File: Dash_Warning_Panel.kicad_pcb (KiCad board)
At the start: 2 copper layers, 60 x 40 mm, 33 parts, among them J1 Conn, U1 TLC6C598, U2 TPS22810

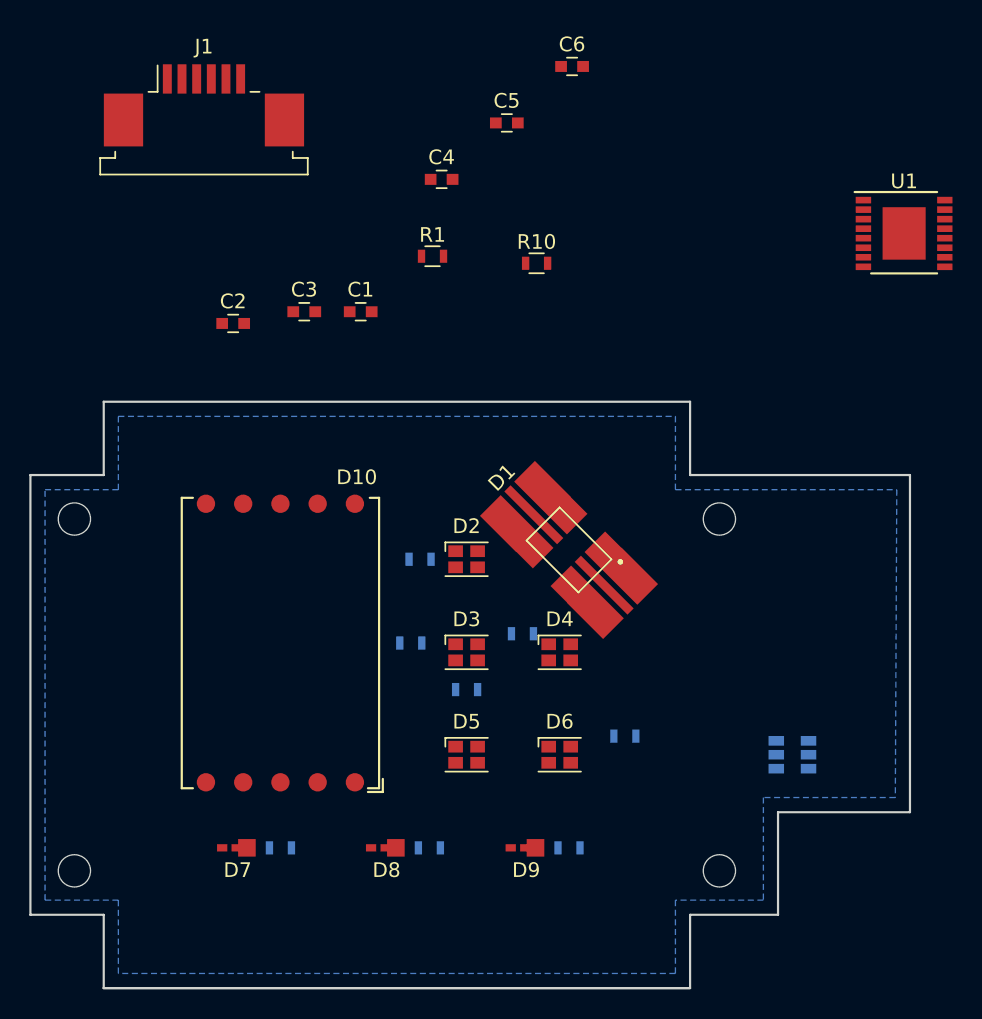
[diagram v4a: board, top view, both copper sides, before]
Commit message: 2020 Initial Design
2020 Initial Design Submission:
Connector changed to 8 pin Molex 90 degree KK
Added Seven Segment Display
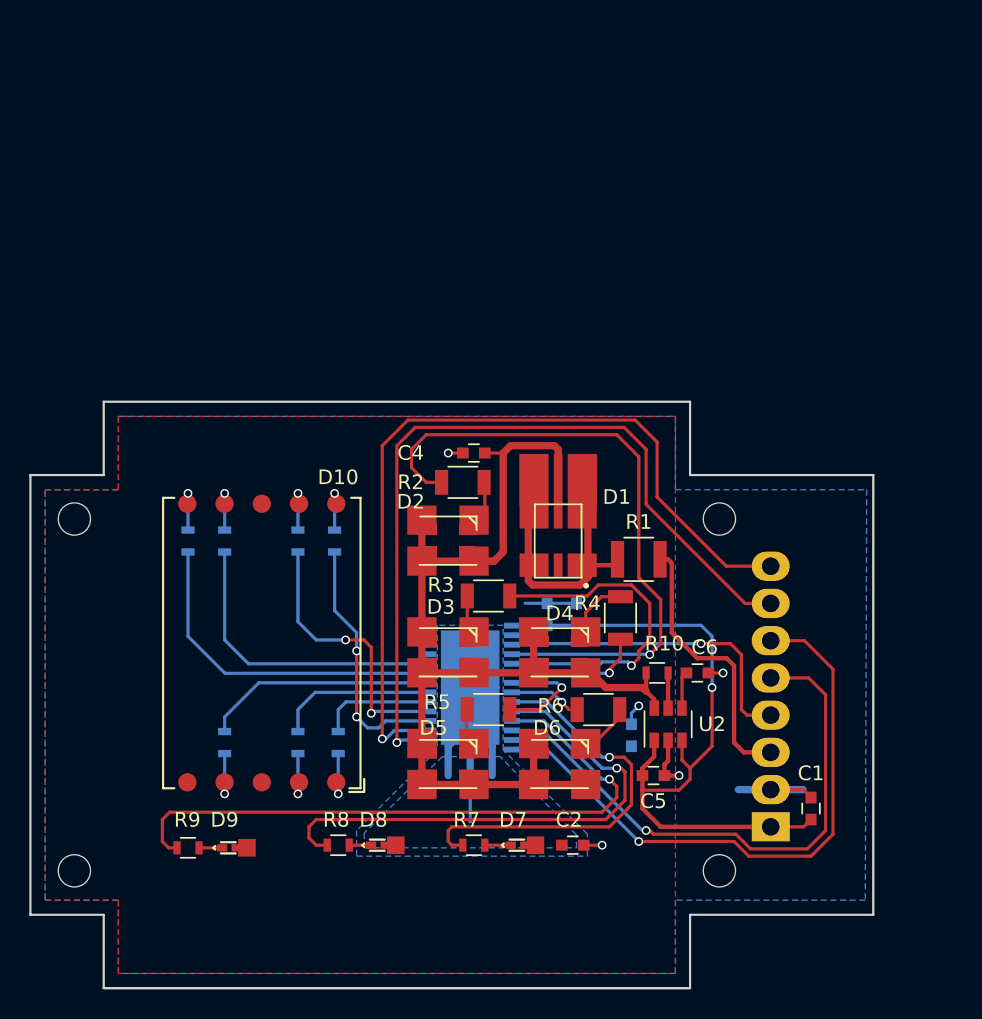
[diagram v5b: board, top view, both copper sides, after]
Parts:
- added C7: 1uF, Capacitors_SMD:C_0603, B.Cu at (206.2, 122.5)
- added C8: 0.1uF, Capacitors_SMD:C_0603, B.Cu at (204.2, 122.5)
- added R11: 116.7, Resistors_SMD:R_0603, B.Cu at (182.2, 117.5)
- added R12: 116.7, Resistors_SMD:R_0603, B.Cu at (179.8, 117.5)
- added R13: 116.7, Resistors_SMD:R_0603, B.Cu at (182.2, 131.2)
- added R14: 116.7, Resistors_SMD:R_0603, B.Cu at (187.2, 131.2)
- added R15: 116.7, Resistors_SMD:R_0603, B.Cu at (190.0, 131.2)
- added R16: 116.7, Resistors_SMD:R_0603, B.Cu at (187.2, 117.5)
- added R17: 116.7, Resistors_SMD:R_0603, B.Cu at (189.8, 117.5)
- C3: moved to B.Cu
- D10: value DSM7T -> DSM7TA56105T
- D2, D3, D4, D5, D6: footprint LEDs:LED_Cree-PLCC4_2x2mm_CW -> OSRAM:OSRAM_PLCC-4_THERM_PAD
- J1: footprint Connectors_TE-Connectivity:TE_84953-6_1x06_P1.0mm_Horizontal -> Molex:Molex_KK-171857_08x2.54mm_Right_Angle; moved to B.Cu
- R1: footprint Resistors_SMD:R_0603 -> Resistors_SMD:R_1210
- R2, R3, R4, R5, R6: footprint Resistors_SMD:R_0603 -> Resistors_SMD:R_1206; moved to F.Cu
- R7: renamed from R9; moved to F.Cu
- R8, U2: moved to F.Cu
- R9: renamed from R7; moved to F.Cu
- U1: value TLC6C598 -> TLC6C5816; footprint Housings_SSOP:TSSOP-16-1EP_4.4x5mm_Pitch0.65mm -> Housings_SSOP:HTSSOP-28_4.4x9.7mm_Pitch0.65mm_ThermalPad; moved to B.Cu
- moved J1 62.6 mm to (219.5, 137.0), turned to 90 degrees
- moved C1 45.7 mm to (222.2, 135.8), turned to 90 degrees
- moved C5 45.6 mm to (211.5, 133.5), turned to 180 degrees
- moved U1 42.8 mm to (199.0, 127.5), turned to 180 degrees
- moved C2 42.5 mm to (206.0, 138.2)
- moved C6 42.2 mm to (214.5, 126.5), turned to 180 degrees
- moved C3 36.5 mm to (210.0, 130.8), turned to 270 degrees
- moved R10 29.1 mm to (211.8, 126.5)
- moved R1 25.0 mm to (210.5, 118.8)
- moved C4 18.8 mm to (199.2, 111.5), turned to 180 degrees
- moved R4 11.6 mm to (209.2, 122.8), turned to 270 degrees
- moved U2 8.73 mm to (212.5, 130.0), turned to 90 degrees
- moved R7 6.49 mm to (199.2, 138.2), turned to 180 degrees
- moved R9 6.31 mm to (179.8, 138.4), turned to 180 degrees
- moved R8 6.22 mm to (190.0, 138.2), turned to 180 degrees
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- renumbered D9 to D7, D7 to D9
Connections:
- net Net-(D1-Pad1) renamed /D1_h
- net Net-(D2-Pad1) renamed /D2_h
- net Net-(D3-Pad1) renamed /D3_h
- net Net-(D4-Pad1) renamed /D4_h
- net Net-(D5-Pad1) renamed /D5_h
- net Net-(D6-Pad1) renamed /D6_h
- C1 pad 2: /GND -> GND
- C2 pad 2: Net-(C2-Pad2) -> GND
- C3 pad 2: Net-(C2-Pad2) -> GND
- C4 pad 2: Net-(C2-Pad2) -> GND
- C5 pad 1: Net-(C2-Pad2) -> GND
- C6 pad 1: Net-(C2-Pad2) -> GND
- D1 pad 2: Net-(D1-Pad2) -> /LED_Power
- D10 pad 1: (no net) -> /e_h
- D10 pad 10: (no net) -> /g_h
- D10 pad 2: (no net) -> /d_h
- D10 pad 3: (no net) -> /LED_Power
- D10 pad 4: (no net) -> /c_h
- D10 pad 5: (no net) -> Net-(D10-Pad5)
- D10 pad 6: (no net) -> /b_h
- D10 pad 7: (no net) -> /a_h
- D10 pad 8: (no net) -> /LED_Power
- D10 pad 9: (no net) -> /f_h
- D2 pad 2: Net-(D2-Pad2) -> /LED_Power
- D3 pad 2: Net-(D3-Pad2) -> /LED_Power
- D4 pad 2: Net-(D4-Pad2) -> /LED_Power
- D5 pad 2: Net-(D5-Pad2) -> /LED_Power
- D6 pad 2: Net-(D6-Pad2) -> /LED_Power
- D7 pad 2: Net-(D9-Pad2) -> /LED_Power
- D8 pad 2: Net-(D8-Pad2) -> /LED_Power
- D9 pad 2: Net-(D7-Pad2) -> /LED_Power
- J1 pad 2: /GND -> GND
- J1 pad 4: /SDI -> /G
- J1 pad 5: /SCLK -> /SDI
- J1 pad 6: /RCLK -> /CLR
- R2 pad 2: Net-(R2-Pad2) -> /D2
- R3 pad 2: Net-(R3-Pad2) -> /D3
- R4 pad 2: Net-(R4-Pad2) -> /D4
- R5 pad 2: Net-(R5-Pad2) -> /D5
- R6 pad 2: Net-(R6-Pad2) -> /D6
- R7 pad 1: Net-(D9-Pad1) -> /D7_h
- R7 pad 2: Net-(R9-Pad2) -> /D7
- R8 pad 1: Net-(D8-Pad1) -> /D8_h
- R8 pad 2: Net-(R8-Pad2) -> /D8
- R9 pad 1: Net-(D7-Pad1) -> /D9_h
- R9 pad 2: Net-(R7-Pad2) -> /D9
- U1 pad 1: Net-(U1-Pad1) -> /VCC
- U1 pad 10: Net-(U1-Pad10) -> /D8
- U1 pad 11: Net-(U1-Pad11) -> /D9
- U1 pad 12: Net-(U1-Pad12) -> /SDI
- U1 pad 13: Net-(U1-Pad13) -> /CLR
- U1 pad 14: Net-(U1-Pad14) -> GND
- U1 pad 16: Net-(U1-Pad16) -> /RCLK
- U1 pad 17: (no net) -> /SCLK
- U1 pad 2: Net-(U1-Pad2) -> /G
- U1 pad 3: Net-(U1-Pad3) -> /G
- U1 pad 4: Net-(U1-Pad4) -> /D2
- U1 pad 5: Net-(U1-Pad5) -> /D3
- U1 pad 6: Net-(U1-Pad6) -> /D4
- U1 pad 7: Net-(U1-Pad7) -> /D5
- U1 pad 8: Net-(U1-Pad8) -> /D6
- U1 pad 9: Net-(U1-Pad9) -> /D7
- U2 pad 2: Net-(C2-Pad2) -> GND
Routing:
- net /LED_Power: track 0.00 -> 77.2 mm, vias 0 -> 1
- net /SCLK: track 0.00 -> 56.9 mm, vias 0 -> 1
- net /RCLK: track 0.00 -> 55.7 mm, vias 0 -> 1
- net /VCC: track 0.00 -> 47.2 mm, vias 0 -> 1
- net /D2: track 0.00 -> 44.1 mm, vias 0 -> 1
- net /D9: track 0.00 -> 44.1 mm, vias 0 -> 1
- net /CLR: track 0.00 -> 42.1 mm, vias 0 -> 1
- net /SDI: track 0.00 -> 38.7 mm, vias 0 -> 1
- net /D8: track 0.00 -> 35.9 mm, vias 0 -> 1
- net /D7: track 0.00 -> 27.7 mm, vias 0 -> 1
- net /D1_h: track 0.00 -> 24.2 mm
- net /G: track 0.00 -> 23.8 mm, vias 0 -> 1
- net /D3: track 0.00 -> 23.5 mm, vias 0 -> 1
- net /b: track 0.00 -> 23.2 mm
- net /a: track 0.00 -> 20.6 mm
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- added copper zone on F.Cu, net /LED_Power
- added copper zone on B.Cu, net GND
- added copper zone on B.Cu, net Net-(U1-Pad26)
- removed copper zone on B.Cu, net /GND
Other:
- board size 60 x 40 mm -> 57.5 x 40 mm
- net class Default: clearance 0.17 -> 0.22; via_dia 0.4 -> 0.6; via_drill 0.3 -> 0.4
- net class Thin added: clearance 0.13, trace_width 0.13, via_dia 0.6, via_drill 0.4
- net class Wide: clearance 0.2 -> 0.22
- rule trace_clearance: 0.17 -> 0.22
- rule trace_min: 0.16 -> 0.127
- rule via_min_drill: 0.3 -> 0.4
- rule via_min_size: 0.4 -> 0.6
- board text added: "Designed by: Alex Podgorski"
- board text added: "SCLK RCLK CLR SDI CONT NEUT GND VCC"
- board text added: "UCONN FSAE 2020"
- board text removed: "CLK SDI SDO MC GND VCC"
- board text removed: "Drive On"
- board text removed: "Power On"
- board text removed: "UCONN FSAE 2019"

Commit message: First Manufacture Ready 2020
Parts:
- D2, D6: value LY E6SF -> SM1206NYC-IL; footprint OSRAM:OSRAM_PLCC-4_THERM_PAD -> LEDs:LED_1206
- D3, D4, D5: value LS E6SF -> SM1206NHC-IL; footprint OSRAM:OSRAM_PLCC-4_THERM_PAD -> LEDs:LED_1206
- D7, D8, D9: value KP DELPS -> SM1206NPGC-IL; footprint OSRAM:PLCC-2 -> LEDs:LED_1206
- J1: footprint Molex:Molex_KK-171857_08x2.54mm_Right_Angle -> FSAE-Dash-Warning-Panel:8wireConn
- R1: value 11.3 -> 11
- R10: value 86.6 -> 120
- R11, R12, R13, R14, R15, R16, R17, R7, R8, R9: value 116.7 -> 120
- R2, R3, R4, R5, R6: value 71 -> 120; footprint Resistors_SMD:R_1206 -> Resistors_SMD:R_0603
- moved R9 5.55 mm to (184.0, 142.0)
- moved C1 5.46 mm to (217.0, 134.2)
- moved R8 4.25 mm to (192.0, 142.0)
- moved C2 4.01 mm to (209.9, 139.2)
- moved R7 3.82 mm to (200.0, 142.0)
- moved D9 3.77 mm to (185.9, 139.1)
- moved R3 2.15 mm to (199.0, 123.0)
- moved J1 2.06 mm to (219.0, 135.0), turned to 0 degrees
- moved D8 1.79 mm to (194.0, 139.1)
- moved R5 1.60 mm to (199.0, 130.0)
- moved R2 1.00 mm to (198.5, 114.5)
- moved R6 1.00 mm to (207.8, 130.0)
- moved D7 0.95 mm to (202.0, 139.2)
- moved R4 0.79 mm to (209.0, 123.5)
- moved D5 0.24 mm to (197.5, 132.5), turned to 180 degrees
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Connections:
- U1 pad 29: Net-(U1-Pad26) -> GND
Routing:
- net GND: track 18.0 -> 76.5 mm
- net /LED_Power: track 77.2 -> 25.8 mm
- net Net-(U1-Pad26): track 16.7 -> 0.00 mm
- net /SDI: track 38.7 -> 30.7 mm
- net /CLR: track 42.1 -> 34.2 mm
- net /VCC: track 47.2 -> 43.5 mm
- net /D2_h: track 2.90 -> 6.03 mm
- net /D3: track 23.5 -> 26.1 mm
- net /D5: track 7.71 -> 10.1 mm
- net /NEUT: track 18.9 -> 16.7 mm
- net /D9: track 44.1 -> 42.0 mm
- net /D9_h: track 1.58 -> 3.30 mm
- net /D7: track 27.7 -> 29.5 mm
- net /D8_h: track 1.49 -> 3.08 mm
- net /G: track 23.8 -> 22.3 mm
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- removed copper zone on B.Cu, net Net-(U1-Pad26)
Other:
- board size 57.5 x 40 mm -> 53 x 40 mm
- board text added: "CLR"
- board text added: "CONT"
- board text added: "GND"
- board text added: "NEUT"
- board text added: "RCLK"
- board text added: "SCLK"
- board text added: "SDI"
- board text added: "VCC"
- board text removed: "M2 2.2mm"
- board text removed: "SCLK RCLK CLR SDI CONT NEUT GND VCC"
- board text removed: "Y"

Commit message: Added LDO 3.3V Reg
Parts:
- added U3: TLV741P, TO_SOT_Packages_SMD:SOT-23-5, B.Cu at (210.8, 122.0)
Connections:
- C7 pad 1: /VCC -> +3V3
- C8 pad 1: /VCC -> +3V3
- U1 pad 1: /VCC -> +3V3
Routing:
- net GND: track 76.5 -> 86.2 mm
- net +3V3: track 0.00 -> 8.72 mm
- net /VCC: track 43.5 -> 37.2 mm
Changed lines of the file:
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@@
     (thickness 1.6)
     (drawings 150)
-    (tracks 326)
+    (tracks 335)
     (zones 0)
-    (modules 42)
-    (nets 48)
+    (modules 43)
+    (nets 50)
   )
   (page A)
@@
   (net 46 "Net-(U1-Pad26)")
   (net 47 "Net-(U1-Pad25)")
+  (net 48 "Net-(U3-Pad4)")
+  (net 49 +3V3)
   (net_class Default "This is the default net class."
     (clearance 0.22)
@@
     (uvia_dia 0.3)
     (uvia_drill 0.1)
+    (add_net +3V3)
     (add_net /CLR)
     (add_net /D1_h)
@@
     (add_net "Net-(U1-Pad26)")
     (add_net "Net-(U1-Pad27)")
+    (add_net "Net-(U3-Pad4)")
   )
   (net_class Thin ""
@@
       (net 26 /G))
     (pad 1 smd rect (at -2.85 4.225 180) (size 1.1 0.4) (layers B.Cu B.Paste B.Mask)
-      (net 3 /VCC))
+      (net 49 +3V3))
     (pad 29 smd rect (at 0 1.905 180) (size 4 4) (layers B.Cu B.Paste B.Mask)
       (net 10 GND))
@@
       (net 10 GND))
     (pad 1 smd rect (at -0.75 0 90) (size 0.8 0.75) (layers B.Cu B.Paste B.Mask)
-      (net 3 /VCC))
+      (net 49 +3V3))
     (model Capacitors_SMD.3dshapes/C_0603.wrl
       (at (xyz 0 0 0))
@@
     (fp_line (start 1.4 -0.65) (end -1.4 -0.65) (layer B.CrtYd) (width 0.05))
     (pad 1 smd rect (at -0.75 0 90) (size 0.8 0.75) (layers B.Cu B.Paste B.Mask)
-      (net 3 /VCC))
+      (net 49 +3V3))
     (pad 2 smd rect (at 0.75 0 90) (size 0.8 0.75) (layers B.Cu B.Paste B.Mask)
       (net 10 GND))
@@
       (net 44 /g))
     (model ${KISYS3DMOD}/Resistors_SMD.3dshapes/R_0603.wrl
+      (at (xyz 0 0 0))
+      (scale (xyz 1 1 1))
+      (rotate (xyz 0 0 0))
+    )
+  )
+  (module TO_SOT_Packages_SMD:SOT-23-5 (layer B.Cu)
+    (at 210.75 122 180)
+    (descr "5-pin SOT23 package")
+    (tags SOT-23-5)
+    (attr smd)
+    (fp_text reference U3 (at 0 2.9) (layer B.SilkS)
+      (effects (font (size 1 1) (thickness 0.15)) (justify mirror))
+    )
+    (fp_text value TLV741P (at 0 -2.9) (layer B.Fab)
+      (effects (font (size 1 1) (thickness 0.15)) (justify mirror))
+    )
+    (fp_line (start 0.9 1.55) (end 0.9 -1.55) (layer B.Fab) (width 0.1))
+    (fp_line (start 0.9 -1.55) (end -0.9 -1.55) (layer B.Fab) (width 0.1))
+    (fp_line (start -0.9 0.9) (end -0.9 -1.55) (layer B.Fab) (width 0.1))
+    (fp_line (start 0.9 1.55) (end -0.25 1.55) (layer B.Fab) (width 0.1))
+    (fp_line (start -0.9 0.9) (end -0.25 1.55) (layer B.Fab) (width 0.1))
+    (fp_line (start -1.9 -1.8) (end -1.9 1.8) (layer B.CrtYd) (width 0.05))
+    (fp_line (start 1.9 -1.8) (end -1.9 -1.8) (layer B.CrtYd) (width 0.05))
+    (fp_line (start 1.9 1.8) (end 1.9 -1.8) (layer B.CrtYd) (width 0.05))
+    (fp_line (start -1.9 1.8) (end 1.9 1.8) (layer B.CrtYd) (width 0.05))
+    (fp_line (start 0.9 1.61) (end -1.55 1.61) (layer B.SilkS) (width 0.12))
+    (fp_line (start -0.9 -1.61) (end 0.9 -1.61) (layer B.SilkS) (width 0.12))
+    (fp_text user %R (at 0 0 270) (layer B.Fab)
+      (effects (font (size 0.5 0.5) (thickness 0.075)) (justify mirror))
+    )
+    (pad 5 smd rect (at 1.1 0.95 180) (size 1.06 0.65) (layers B.Cu B.Paste B.Mask)
+      (net 49 +3V3))
+    (pad 4 smd rect (at 1.1 -0.95 180) (size 1.06 0.65) (layers B.Cu B.Paste B.Mask)
+      (net 48 "Net-(U3-Pad4)"))
+    (pad 3 smd rect (at -1.1 -0.95 180) (size 1.06 0.65) (layers B.Cu B.Paste B.Mask)
+      (net 3 /VCC))
+    (pad 2 smd rect (at -1.1 0 180) (size 1.06 0.65) (layers B.Cu B.Paste B.Mask)
+      (net 10 GND))
+    (pad 1 smd rect (at -1.1 0.95 180) (size 1.06 0.65) (layers B.Cu B.Paste B.Mask)
+      (net 3 /VCC))
+    (model ${KISYS3DMOD}/TO_SOT_Packages_SMD.3dshapes/SOT-23-5.wrl
       (at (xyz 0 0 0))
       (scale (xyz 1 1 1))
@@
   (segment (start 213.25 134.5) (end 210.75 134.5) (width 0.22) (layer F.Cu) (net 3))
   (segment (start 210.75 134.5) (end 210.75 133.5) (width 0.3) (layer F.Cu) (net 3))
-  (segment (start 204.225 123.275) (end 204.25 123.25) (width 0.22) (layer B.Cu) (net 3))
-  (segment (start 201.85 123.275) (end 204.225 123.275) (width 0.22) (layer B.Cu) (net 3))
-  (segment (start 204.25 123.25) (end 206.25 123.25) (width 0.22) (layer B.Cu) (net 3))
-  (segment (start 206.25 123.25) (end 213.5 123.25) (width 0.22) (layer B.Cu) (net 3))
-  (segment (start 213.5 123.25) (end 214.75 123.25) (width 0.22) (layer B.Cu) (net 3))
   (via (at 215.5 127.5) (size 0.6) (drill 0.4) (layers F.Cu B.Cu) (net 3))
-  (segment (start 214.75 123.25) (end 215.5 124) (width 0.22) (layer B.Cu) (net 3))
-  (segment (start 215.5 124) (end 215.5 127.5) (width 0.22) (layer B.Cu) (net 3))
   (segment (start 215.5 127.5) (end 215.5 131.5) (width 0.22) (layer F.Cu) (net 3))
   (segment (start 215.5 131.5) (end 214 133) (width 0.22) (layer F.Cu) (net 3))
@@
   (segment (start 219 135) (end 216.75 135) (width 0.3) (layer F.Cu) (net 3))
   (segment (start 216.75 135) (end 215.75 136) (width 0.3) (layer F.Cu) (net 3))
+  (segment (start 215.5 124) (end 215.5 127.5) (width 0.22) (layer B.Cu) (net 3))
+  (segment (start 211.85 121.05) (end 211.2 121.05) (width 0.22) (layer B.Cu) (net 3))
+  (segment (start 211.2 121.05) (end 210.75 121.5) (width 0.22) (layer B.Cu) (net 3))
+  (segment (start 210.75 121.5) (end 210.75 122.5) (width 0.22) (layer B.Cu) (net 3))
+  (segment (start 211.2 122.95) (end 211.85 122.95) (width 0.22) (layer B.Cu) (net 3))
+  (segment (start 210.75 122.5) (end 211.2 122.95) (width 0.22) (layer B.Cu) (net 3))
+  (segment (start 214.45 122.95) (end 215.5 124) (width 0.22) (layer B.Cu) (net 3))
+  (segment (start 211.85 122.95) (end 214.45 122.95) (width 0.22) (layer B.Cu) (net 3))
   (segment (start 213.45 126.8) (end 213.75 126.5) (width 0.22) (layer F.Cu) (net 4))
   (segment (start 213.45 128.9) (end 213.45 126.8) (width 0.22) (layer F.Cu) (net 4))
@@
   (segment (start 194.5 121.5) (end 194.7 121.3) (width 0.22) (layer B.Cu) (net 10))
   (segment (start 194.7 121.3) (end 203 121.3) (width 0.8) (layer B.Cu) (net 10))
+  (segment (start 211.85 122) (end 213.25 122) (width 0.3) (layer B.Cu) (net 10))
+  (segment (start 194.7 133.25) (end 203 133.25) (width 0.8) (layer B.Cu) (net 10))
   (segment (start 202.968 115.849) (end 202.968 119.151) (width 0.5) (layer F.Cu) (net 11))
   (segment (start 207.032 119.151) (end 207.032 115.849) (width 0.5) (layer F.Cu) (net 11))
@@
   (segment (start 210 120.5) (end 211.25 121.75) (width 0.22) (layer F.Cu) (net 28))
   (segment (start 211.25 121.75) (end 211.25 124.25) (width 0.22) (layer F.Cu) (net 28))
+  (segment (start 208.5 126.5) (end 208.475 126.525) (width 0.22) (layer B.Cu) (net 29))
   (segment (start 208.475 126.525) (end 201.85 126.525) (width 0.22) (layer B.Cu) (net 29))
-  (segment (start 208.5 126.5) (end 208.475 126.525) (width 0.22) (layer B.Cu) (net 29))
+  (segment (start 208.5 126.25) (end 208.5 126.5) (width 0.22) (layer F.Cu) (net 29))
+  (segment (start 209 125.75) (end 208.5 126.25) (width 0.22) (layer F.Cu) (net 29))
+  (segment (start 209 124.25) (end 209 125.75) (width 0.22) (layer F.Cu) (net 29))
   (via (at 208.5 126.5) (size 0.6) (drill 0.4) (layers F.Cu B.Cu) (net 29))
-  (segment (start 208.5 126.25) (end 208.5 126.5) (width 0.22) (layer F.Cu) (net 29))
-  (segment (start 209 124.25) (end 209 125.75) (width 0.22) (layer F.Cu) (net 29))
-  (segment (start 209 125.75) (end 208.5 126.25) (width 0.22) (layer F.Cu) (net 29))
   (via (at 205.25 127.5) (size 0.6) (drill 0.4) (layers F.Cu B.Cu) (net 30))
   (segment (start 204.925 127.175) (end 201.85 127.175) (width 0.22) (layer B.Cu) (net 30))
@@
   (segment (start 196.15 129.775) (end 193.225 129.775) (width 0.22) (layer B.Cu) (net 44))
   (segment (start 193.225 129.775) (end 192.75 130.25) (width 0.22) (layer B.Cu) (net 44))
+  (segment (start 204.225 123.275) (end 204.25 123.25) (width 0.22) (layer B.Cu) (net 49))
+  (segment (start 201.85 123.275) (end 204.225 123.275) (width 0.22) (layer B.Cu) (net 49))
+  (segment (start 204.25 123.25) (end 206.25 123.25) (width 0.22) (layer B.Cu) (net 49))
+  (segment (start 209.65 121.05) (end 208.7 121.05) (width 0.22) (layer B.Cu) (net 49))
+  (segment (start 206.5 123.25) (end 206.25 123.25) (width 0.22) (layer B.Cu) (net 49))
+  (segment (start 208.7 121.05) (end 206.5 123.25) (width 0.22) (layer B.Cu) (net 49))
   (zone (net 10) (net_name GND) (layer B.Cu) (hatch edge 0.508)
     (connect_pads (clearance 0.3))
@@
       )
     )
+  )
+  (zone (net 0) (net_name "") (layer B.Cu) (hatch edge 0.508)
+    (connect_pads (clearance 0.3))
+    (min_thickness 0.254)
+    (keepout (tracks allowed) (vias allowed) (copperpour not_allowed))
+    (fill (arc_segments 32) (thermal_gap 0.508) (thermal_bridge_width 0.508))
+    (polygon
+      (pts
+        (xy 212.5 120.5) (xy 209 120.5) (xy 209 123.75) (xy 212.5 123.75)
+      )
+    )

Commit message: Release Candidate 1
Fixed Blue LED ambiguity
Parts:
- moved D1 0.30 mm to (205.0, 117.2), turned to 180 degrees
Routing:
- net /D1_h: track 24.2 -> 6.51 mm
- net /LED_Power: track 25.8 -> 25.2 mm, vias 1 -> 3
- net /D3: track 26.1 -> 25.5 mm
